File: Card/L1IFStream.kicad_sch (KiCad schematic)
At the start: 107 parts, among them J1 Conn_Coaxial, J2 USB_A, J3 RF_Shield_One_Piece, J4 Conn_Coaxial, U1 MAX2769ETI+T, U10 74LVC374, U11 74HC2GU04, U2 TPS717285DCKR, U3 TPS717285DCKR, U4 NCP164CSN330T1G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

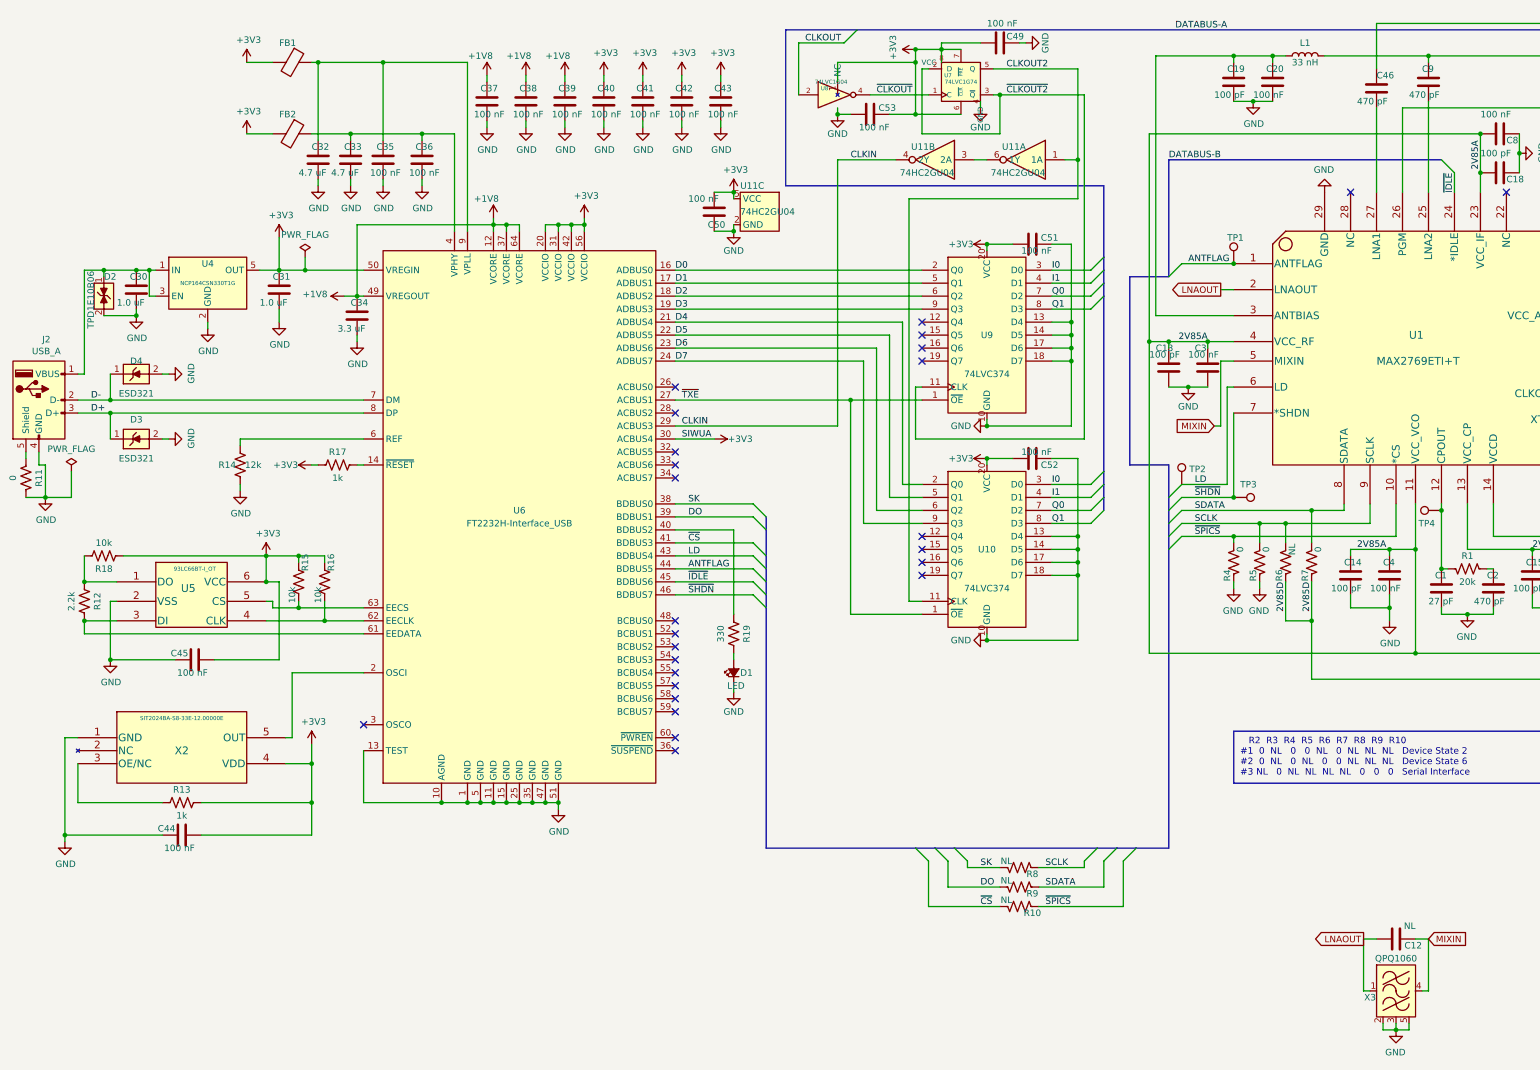
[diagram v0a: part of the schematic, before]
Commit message: Need to rework the symbol library
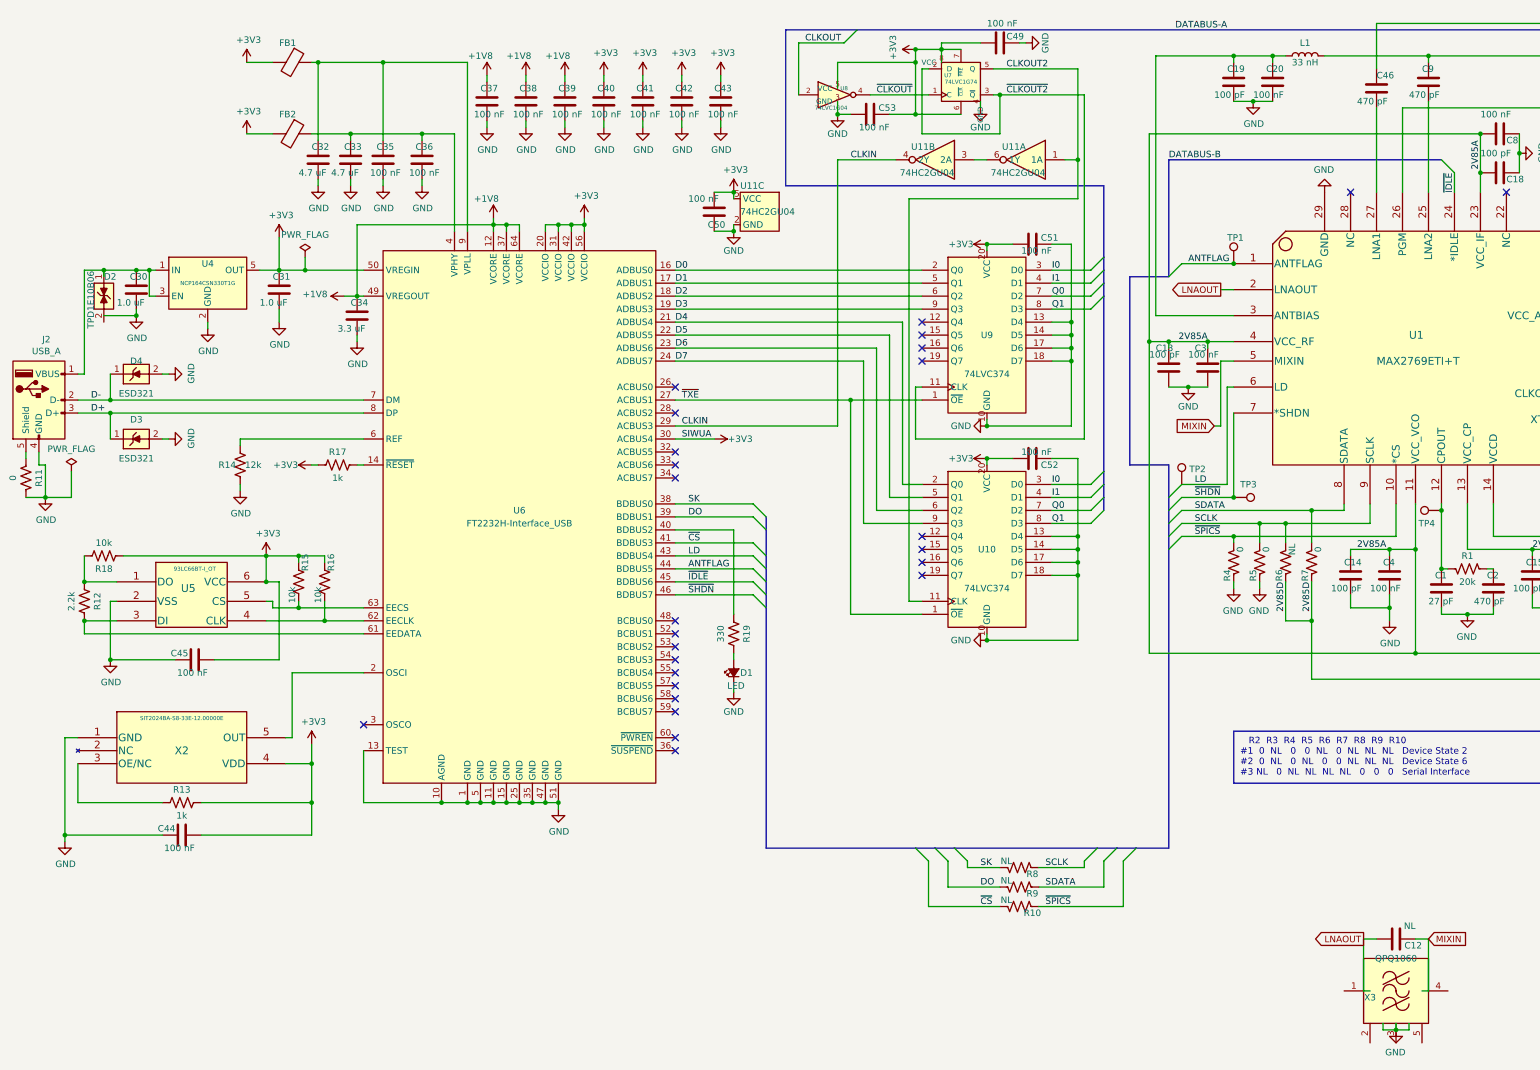
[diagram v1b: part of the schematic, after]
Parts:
- removed U8: 74LVC1G04, L1IFStream:SOT-353_SC-70-5, symbol L1IFStream-rescue:74LVC1G04-MAX2769FT2232H
- added U8: 74LVC1G04, L1IFStream:SOT-353_SC-70-5, symbol L1IFStream:74LVC1G04
- D2: footprint L1IFStream:Texas_DPY0002A_0.6x1mm_P0.65mm -> Package_SON:Texas_DPY0002A_0.6x1mm_P0.65mm
- D3, D4: footprint L1IFStream:DPY-PX1SON_1.0mmx0.6mm -> Diode_SMD:D_0402_1005Metric
- U11: symbol L1IFStream-rescue:74HC2G04-MAX2769FT2232H -> L1IFStream:74HC2UG04; MPN 74HC2GU04GW,125 -> 74HC2G04GW,125; Notes (none) -> Is this supposed to be non-inverting?; Vendor P/N# 1727-6915-6-ND -> 1727-6045-1-ND
- X1: footprint L1IFStream:10L_CQFN -> MAX2769FT2232H:10L_CQFN
- X3: footprint L1IFStream:QPQ1060_1.4x1.2 -> MAX2769FT2232H:Filter_SAW-5_1.4x1.2mm
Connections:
- net +3V3: now also U8.5 (VCC)
- net CLKOUT: now also U8.2
- net GND: now also U8.3 (GND); no longer D2.2 (A), X3.2 (GND), X3.3 (GND), X3.5 (GND)
- net LNAOUT: no longer X3.1 (IN)
- net MIXIN: no longer X3.4 (OUT)
- net ~{CLKOUT}: now also U8.4
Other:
- moved on the sheet: X3
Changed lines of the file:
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@@
     (stroke (width 0) (type default))
   )
+  (wire (pts (xy 176.53 21.59) (xy 176.53 26.67))
+    (stroke (width 0) (type default))
+  )
   (wire (pts (xy 208.28 35.56) (xy 193.04 35.56))
     (stroke (width 0) (type default))
@@
     (stroke (width 0) (type default))
   )
-  (wire (pts (xy 176.53 25.4) (xy 176.53 21.59))
-    (stroke (width 0) (type default))
-  )
   (wire (pts (xy 115.57 25.4) (xy 115.57 24.13))
     (stroke (width 0) (type default))
@@
     (stroke (width 0) (type default))
   )
-  (wire (pts (xy 176.53 30.48) (xy 176.53 31.75))
+  (wire (pts (xy 176.53 29.21) (xy 176.53 31.75))
     (stroke (width 0) (type default))
   )
@@
     )
   )
-  (symbol (lib_name "74HC2G04-MAX2769FT2232H_2") (lib_id "L1IFStream-rescue:74HC2G04-MAX2769FT2232H") (at 213.36 40.64 0) (mirror y) (unit 1)
+  (symbol (lib_id "L1IFStream:74HC2UG04") (at 213.36 40.64 0) (mirror y) (unit 1)
     (in_bom yes) (on_board yes) (dnp no)
     (property "Reference" "U11" (at 213.36 38.1 0)
@@
       (effects (font (size 1.27 1.27)) hide)
     )
-    (property "MPN" "74HC2GU04GW,125" (at 214.63 53.34 0)
+    (property "MPN" "74HC2G04GW,125" (at 214.63 53.34 0)
       (effects (font (size 1.27 1.27)) hide)
     )
-    (property "Notes" "" (at 213.36 50.8 0)
+    (property "Notes" "Is this supposed to be non-inverting?" (at 213.36 50.8 0)
       (effects (font (size 1.27 1.27)) hide)
     )
@@
       (effects (font (size 1.27 1.27)) hide)
     )
-    (property "Vendor P/N#" "1727-6915-6-ND" (at 214.63 58.42 0)
+    (property "Vendor P/N#" "1727-6045-1-ND" (at 214.63 58.42 0)
       (effects (font (size 1.27 1.27)) hide)
     )
@@
     )
   )
-  (symbol (lib_name "74HC2G04-MAX2769FT2232H_1") (lib_id "L1IFStream-rescue:74HC2G04-MAX2769FT2232H") (at 195.58 40.64 0) (mirror y) (unit 2)
+  (symbol (lib_id "L1IFStream:74HC2UG04") (at 195.58 40.64 0) (mirror y) (unit 2)
     (in_bom yes) (on_board yes) (dnp no)
     (property "Reference" "U11" (at 195.58 38.1 0)
@@
       (effects (font (size 1.27 1.27)) hide)
     )
-    (property "MPN" "74HC2GU04GW,125" (at 196.85 53.34 0)
+    (property "MPN" "74HC2G04GW,125" (at 196.85 53.34 0)
       (effects (font (size 1.27 1.27)) hide)
     )
@@
       (effects (font (size 1.27 1.27)) hide)
     )
-    (property "Vendor P/N#" "1727-6915-6-ND" (at 196.85 58.42 0)
+    (property "Vendor P/N#" "1727-6045-1-ND" (at 196.85 58.42 0)
       (effects (font (size 1.27 1.27)) hide)
     )
-    (property "Notes" "" (at 195.58 50.8 0)
+    (property "Notes" "Is this supposed to be non-inverting?" (at 195.58 50.8 0)
       (effects (font (size 1.27 1.27)) hide)
     )
@@
     )
   )
-  (symbol (lib_id "L1IFStream-rescue:74HC2G04-MAX2769FT2232H") (at 161.29 50.8 0) (unit 3)
+  (symbol (lib_id "L1IFStream:74HC2UG04") (at 161.29 50.8 0) (unit 3)
     (in_bom yes) (on_board yes) (dnp no)
     (property "Reference" "U11" (at 157.48 45.72 0)
@@
       (effects (font (size 1.27 1.27)) hide)
     )
-    (property "MPN" "74HC2GU04GW,125" (at 160.02 63.5 0)
+    (property "MPN" "74HC2G04GW,125" (at 160.02 63.5 0)
       (effects (font (size 1.27 1.27)) hide)
     )
@@
       (effects (font (size 1.27 1.27)) hide)
     )
-    (property "Vendor P/N#" "1727-6915-6-ND" (at 160.02 68.58 0)
+    (property "Vendor P/N#" "1727-6045-1-ND" (at 160.02 68.58 0)
       (effects (font (size 1.27 1.27)) hide)
     )
-    (property "Notes" "" (at 161.29 60.96 0)
+    (property "Notes" "Is this supposed to be non-inverting?" (at 161.29 60.96 0)
       (effects (font (size 1.27 1.27)) hide)
     )
@@
     )
   )
-  (symbol (lib_id "L1IFStream-rescue:74LVC1G04-MAX2769FT2232H") (at 176.53 27.94 0) (unit 1)
-    (in_bom yes) (on_board yes) (dnp no)
-    (property "Reference" "U8" (at 173.99 26.67 0)
-      (effects (font (size 0.7874 0.7874)))
-    )
-    (property "Value" "74LVC1G04" (at 175.26 25.4 0)
-      (effects (font (size 0.7874 0.7874)))
-    )
-    (property "Footprint" "L1IFStream:SOT-353_SC-70-5" (at 176.53 27.94 0)
-      (effects (font (size 1.27 1.27)) hide)
-    )
-    (property "Datasheet" "https://assets.nexperia.com/documents/data-sheet/74LVC1G04.pdf" (at 176.53 27.94 0)
-      (effects (font (size 1.27 1.27)) hide)
-    )
-    (property "Description" "IC INVERTER 1CH 1-INP 5TSSOP" (at 176.53 27.94 0)
-      (effects (font (size 1.27 1.27)) hide)
-    )
-    (property "Manufacturer" "Nexperia" (at 176.53 27.94 0)
-      (effects (font (size 1.27 1.27)) hide)
-    )
-    (property "MPN" "74LVC1G04GW,125" (at 176.53 27.94 0)
-      (effects (font (size 1.27 1.27)) hide)
-    )
-    (property "Vendor" "DigiKey" (at 176.53 27.94 0)
-      (effects (font (size 1.27 1.27)) hide)
-    )
-    (property "Vendor P/N#" "1727-2871-1-ND" (at 176.53 27.94 0)
-      (effects (font (size 1.27 1.27)) hide)
-    )
-    (property "Notes" "" (at 176.53 27.94 0)
-      (effects (font (size 1.27 1.27)) hide)
-    )
-    (pin "1")
-    (pin "2")
-    (pin "3")
-    (pin "4")
-    (pin "5")
-    (instances
-      (project "L1IFStream"
-        (path "/e22d8814-0b83-456b-8939-db783783fcf1"
-          (reference "U8") (unit 1)
-        )
-      )
-    )
-  )
   (symbol (lib_id "L1IFStream-rescue:R_US-MAX2769FT2232H") (at 212.09 179.07 270) (mirror x) (unit 1)
     (in_bom yes) (on_board yes) (dnp no)
@@
       (effects (font (size 1.27 1.27)))
     )
-    (property "Footprint" "L1IFStream:DPY-PX1SON_1.0mmx0.6mm" (at 40.64 89.535 0)
+    (property "Footprint" "Diode_SMD:D_0402_1005Metric" (at 40.64 89.535 0)
       (effects (font (size 1.27 1.27)) (justify left) hide)
     )
@@
       (effects (font (size 1.27 1.27)))
     )
-    (property "Footprint" "L1IFStream:DPY-PX1SON_1.0mmx0.6mm" (at 40.64 76.835 0)
+    (property "Footprint" "Diode_SMD:D_0402_1005Metric" (at 40.64 76.835 0)
       (effects (font (size 1.27 1.27)) (justify left) hide)
     )
@@
       (effects (font (size 1.27 1.27)) hide)
     )
-    (property "Datasheet" "https://www.digikey.com/en/products/detail/qt-brightek-qtb/QBLP601-AG1-2943/14664280" (at 156.21 140.97 90)
+    (property "Datasheet" "~" (at 156.21 140.97 90)
       (effects (font (size 1.27 1.27)) hide)
     )
@@
       (effects (font (size 1.27 1.27)) (justify left))
     )
-    (property "Footprint" "L1IFStream:Texas_DPY0002A_0.6x1mm_P0.65mm" (at 38.735 68.58 0)
+    (property "Footprint" "Package_SON:Texas_DPY0002A_0.6x1mm_P0.65mm" (at 38.735 68.58 0)
       (effects (font (size 1.27 1.27)) (justify left) hide)
     )
@@
     )
   )
+  (symbol (lib_id "L1IFStream:74LVC1G04") (at 176.53 27.94 0) (unit 1)
+    (in_bom yes) (on_board yes) (dnp no)
+    (property "Reference" "U8" (at 177.8 26.67 0)
+      (effects (font (size 0.7874 0.7874)))
+    )
+    (property "Value" "74LVC1G04" (at 175.26 30.48 0)
+      (effects (font (size 0.7874 0.7874)))
+    )
+    (property "Footprint" "L1IFStream:SOT-353_SC-70-5" (at 175.26 17.78 0)
+      (effects (font (size 1.27 1.27)) hide)
+    )
+    (property "Datasheet" "https://assets.nexperia.com/documents/data-sheet/74LVC1G04.pdf" (at 175.26 20.32 0)
+      (effects (font (size 1.27 1.27)) hide)
+    )
+    (property "Description" "IC INVERTER 1CH 1-INP 5TSSOP" (at 172.72 13.97 0)
+      (effects (font (size 1.27 1.27)) hide)
+    )
+    (property "Manufacturer" "Nexperia" (at 176.53 5.08 0)
+      (effects (font (size 1.27 1.27)) hide)
+    )
+    (property "MPN" "74LVC1G04GW,125" (at 176.53 7.62 0)
+      (effects (font (size 1.27 1.27)) hide)
+    )
+    (property "Vendor" "DigiKey" (at 176.53 43.18 0)
+      (effects (font (size 1.27 1.27)) hide)
+    )
+    (property "Vendor P/N#" "1727-2871-1-ND" (at 175.26 45.72 0)
+      (effects (font (size 1.27 1.27)) hide)
+    )
+    (property "Notes" "" (at 176.53 27.94 0)
+      (effects (font (size 1.27 1.27)) hide)
+    )
+    (pin "1")
+    (pin "2")
+    (pin "3")
+    (pin "4")
+    (pin "5")
+    (instances
+      (project "L1IFStream"
+        (path "/e22d8814-0b83-456b-8939-db783783fcf1"
+          (reference "U8") (unit 1)
+        )
+      )
+    )
+  )
   (symbol (lib_id "L1IFStream:QPQ1060") (at 285.75 203.2 0) (unit 1)
     (in_bom yes) (on_board yes) (dnp no)
@@
       (effects (font (size 1.27 1.27)))
     )
-    (property "Footprint" "L1IFStream:QPQ1060_1.4x1.2" (at 285.75 191.77 0)
+    (property "Footprint" "MAX2769FT2232H:Filter_SAW-5_1.4x1.2mm" (at 285.75 191.77 0)
       (effects (font (size 1.27 1.27)) hide)
     )
@@
       (effects (font (size 1.524 1.524)))
     )
-    (property "Footprint" "L1IFStream:10L_CQFN" (at 374.65 102.87 0)
+    (property "Footprint" "MAX2769FT2232H:10L_CQFN" (at 374.65 102.87 0)
       (effects (font (size 1.524 1.524)) hide)
     )

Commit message: Added STEP files for some parts
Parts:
- U4: Alternate (none) -> https://www.diodes.com/assets/Datasheets/AP2127.pdf; Notes (none) -> Alternate: AP2127K-ADJTRG1DIDKR-ND
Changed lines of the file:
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@@
       (effects (font (size 1.27 1.27)) hide)
     )
-    (property "Notes" "" (at 53.34 64.77 0)
+    (property "Notes" "Alternate: AP2127K-ADJTRG1DIDKR-ND" (at 53.34 64.77 0)
       (effects (font (size 1.27 1.27)) hide)
     )
+    (property "Alternate" "https://www.diodes.com/assets/Datasheets/AP2127.pdf" (at 53.34 64.77 0)
+      (effects (font (size 1.27 1.27)) hide)
+    )

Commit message: Sent parts to PCBway
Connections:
- net GND: now also X3.2 (GND), X3.3 (GND), X3.5 (GND)
- net LNAOUT: now also X3.1 (IN)
- net MIXIN: now also X3.4 (OUT)
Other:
- moved on the sheet: X3

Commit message: Rotated schematic -- updated some footprints to use local library
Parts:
- D2: footprint Package_SON:Texas_DPY0002A_0.6x1mm_P0.65mm -> L1IFStream:Texas_DPY0002A_0.6x1mm_P0.65mm
- D3, D4: footprint Diode_SMD:D_0402_1005Metric -> L1IFStream:DPY-PX1SON_1.0mmx0.6mm
- X1: footprint MAX2769FT2232H:10L_CQFN -> L1IFStream:10L_CQFN
- X3: footprint MAX2769FT2232H:Filter_SAW-5_1.4x1.2mm -> L1IFStream:QPQ1060_1.4x1.2
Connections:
- net Q0 is gone; now on net ANTBIAS: U1.18 (Q0), U10.7 (D2), U9.7 (D2)
- net Q1 is gone; now on net ANTBIAS: U1.17 (Q1), U10.8 (D3), U9.8 (D3)
- net 2V85D: now also C17.2, C7.2, R2.1; no longer C17.1, C7.1, R2.2
- net GND: now also C17.1, C7.1, D2.2 (A); no longer C17.2, C7.2
- net LNA2: now reaches C9.2, U1.25 (LNA2)
- net ANTBIAS: now reaches C19.1, C20.1, L1.1, U1.3 (ANTBIAS)
- net at R3.2, U1.26 (PGM): now also R2.2; no longer R2.1
- net LNA1: now reaches C46.2, U1.27 (LNA1)
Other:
- moved on the sheet: C11, C12, C13, C19, C20, C21, C22, C23, C24, C3, C46, C47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
